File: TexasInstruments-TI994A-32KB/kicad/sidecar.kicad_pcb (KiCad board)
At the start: 2 copper layers, 57 x 26.5 mm, 9 parts, among them J2 Conn_02x22_Odd_Even, U1 CY62256-70PC, U2 ATF1502AS

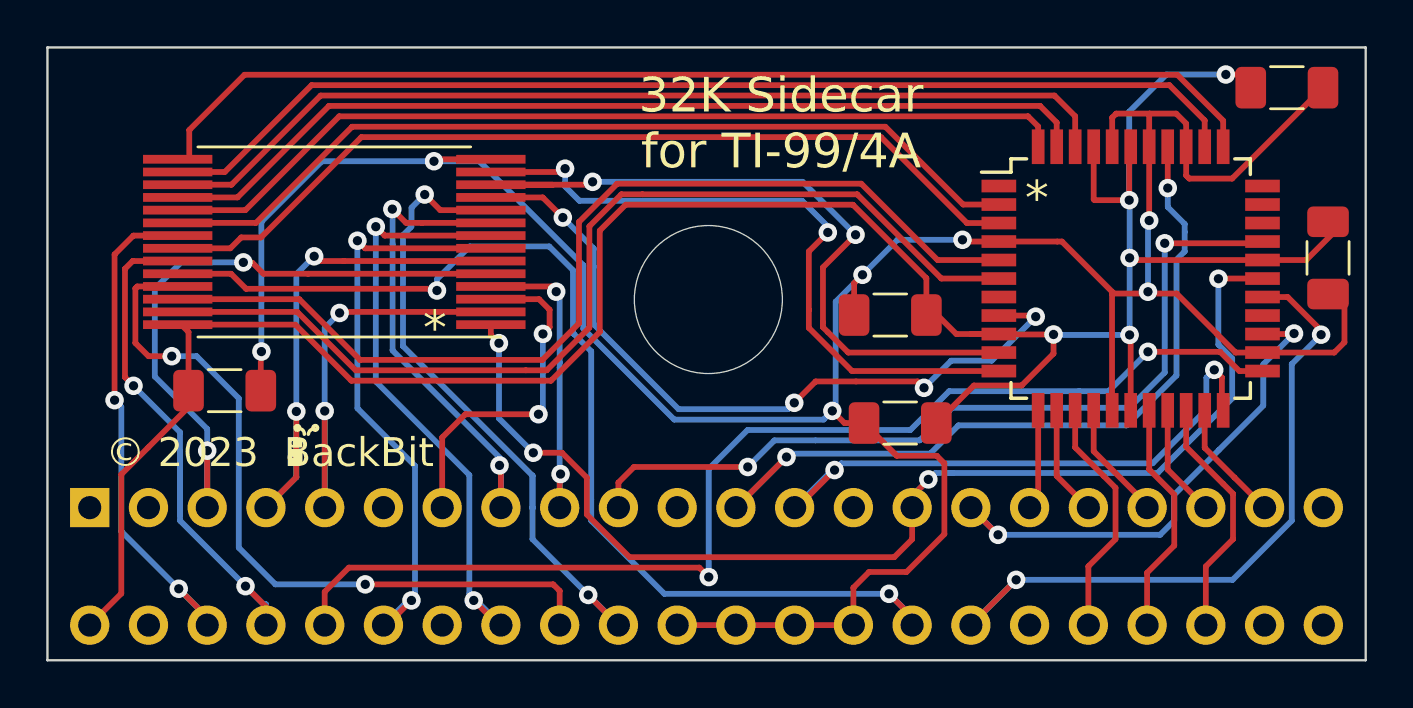
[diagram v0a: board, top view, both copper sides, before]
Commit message: restored sop memory
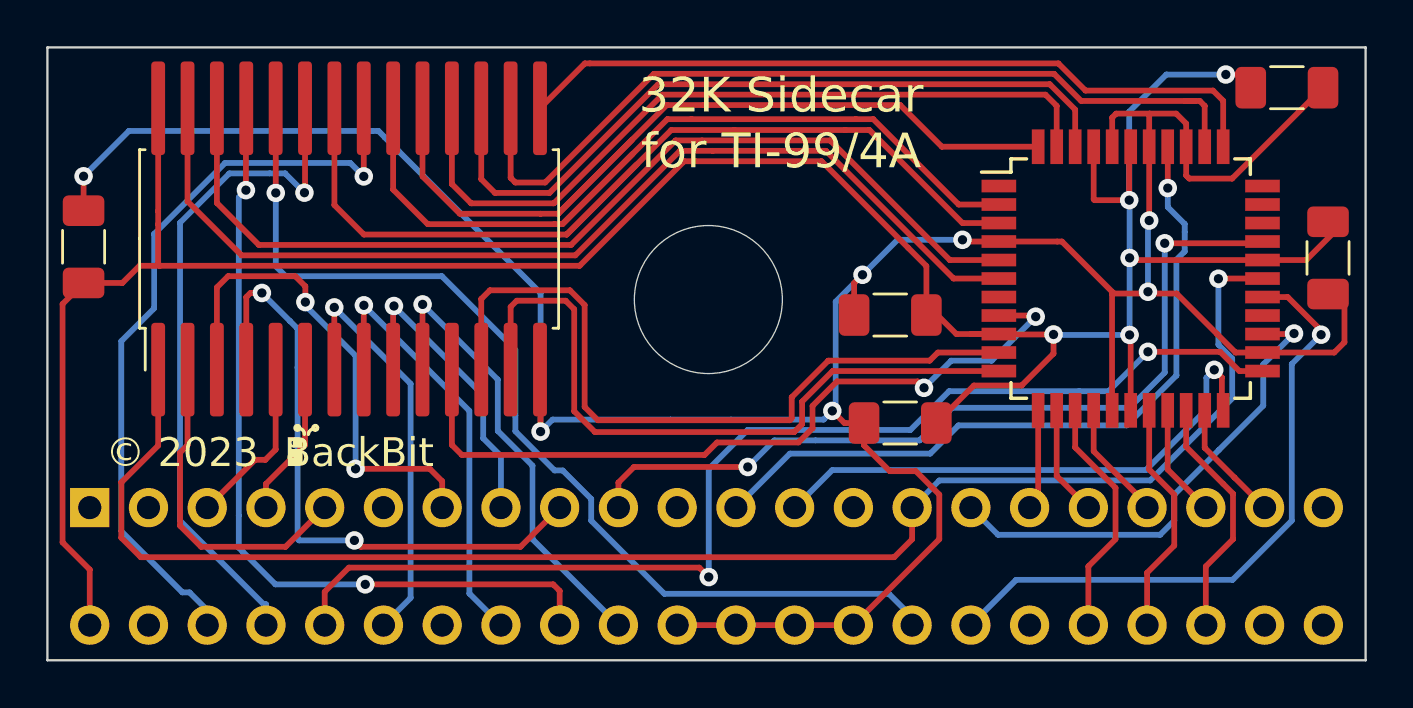
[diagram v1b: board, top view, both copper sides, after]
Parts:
- U1: footprint Package_SO:TSOP-I-28_11.8x8mm_P0.55mm -> Package_SO:SOIC-28W_7.5x17.9mm_P1.27mm
- moved C1 8.71 mm to (118.9, 81.9), turned to 90 degrees
- moved U1 0.65 mm to (130.3, 81.6), turned to 90 degrees
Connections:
- J2 pad 1: SBE -> (no net)
- J2 pad 11: READY -> (no net)
- J2 pad 14: ~{LOAD} -> (no net)
- J2 pad 21: ~{CRUCLK} -> (no net)
- J2 pad 27: ~{MBE} -> (no net)
- J2 pad 3: ~{EXTINT} -> (no net)
- J2 pad 34: CRUIN -> (no net)
- J2 pad 4: ~{RESET} -> (no net)
- J2 pad 42: IAQ -> (no net)
- J2 pad 43: AUDIN -> (no net)
- J2 pad 44: unconnected-(J2-Pad44) -> (no net)
- U2 pad 1: TDI -> (no net)
- U2 pad 26: TCK -> (no net)
- U2 pad 31: unconnected-(U2-Pad31) -> (no net)
- U2 pad 32: TDO -> (no net)
- U2 pad 33: unconnected-(U2-Pad33) -> (no net)
- U2 pad 7: TMS -> (no net)
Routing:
- net A10: track 27.8 -> 7.72 mm, vias 2 -> 0
- net A11: track 23.7 -> 6.67 mm, vias 2 -> 0
- net Q4: track 48.9 -> 33.0 mm
- net A1: track 52.4 -> 67.3 mm, vias 4 -> 1
- net A9: track 13.8 -> 27.3 mm
- net Q3: track 47.2 -> 36.8 mm
- net Q2: track 41.6 -> 32.0 mm
- net A15: track 28.7 -> 20.2 mm, vias 2 -> 1
- net A5: track 23.3 -> 31.7 mm, vias 2 -> 1
- net Q1: track 40.5 -> 32.7 mm
- net VCC: track 108.9 -> 116.5 mm
- net A14: track 20.7 -> 13.4 mm, vias 2 -> 1
- net A12: track 25.3 -> 18.3 mm, vias 2 -> 1
- net A13: track 25.7 -> 19.1 mm, vias 2 -> 1
- net A8: track 15.1 -> 21.7 mm
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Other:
- board text removed: "*"
